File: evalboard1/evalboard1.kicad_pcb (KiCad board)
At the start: 2 copper layers, 67.5 x 45.3 mm, 36 parts, among them J1 USB_OTG, J10 Conn_01x12_Male, J11 Conn_01x18_Male, J12 Conn_01x15_Male, J13 Conn_01x03_Male, J14 power select, J2 RX, J3 TX, J4 analog, J5 IO, J6 core, J7 Conn_01x09_Male, J8 Conn_01x06_Male, J9 Conn_01x17_Male, SW1 SW_Push, U1 GA144A12, U2 FT234XD-R, U3 LTC3406ES5-1.8, U4 SST25WF080B, Y1 Crystal

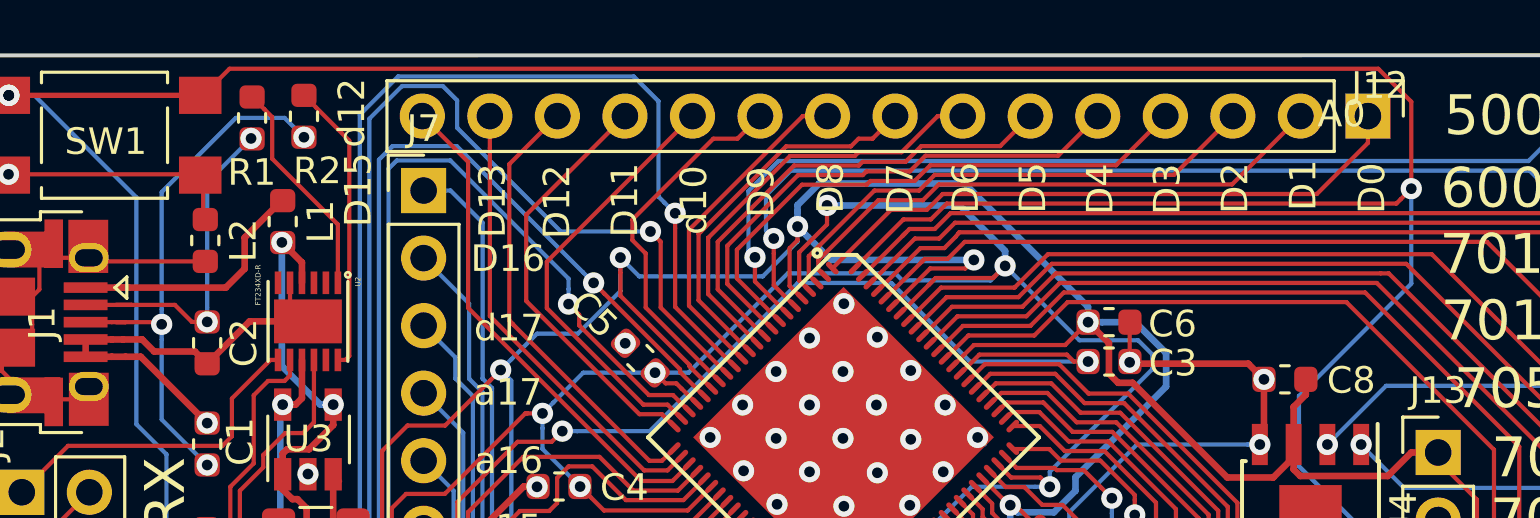
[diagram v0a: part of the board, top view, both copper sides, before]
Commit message: add pull-up resistor on RESET
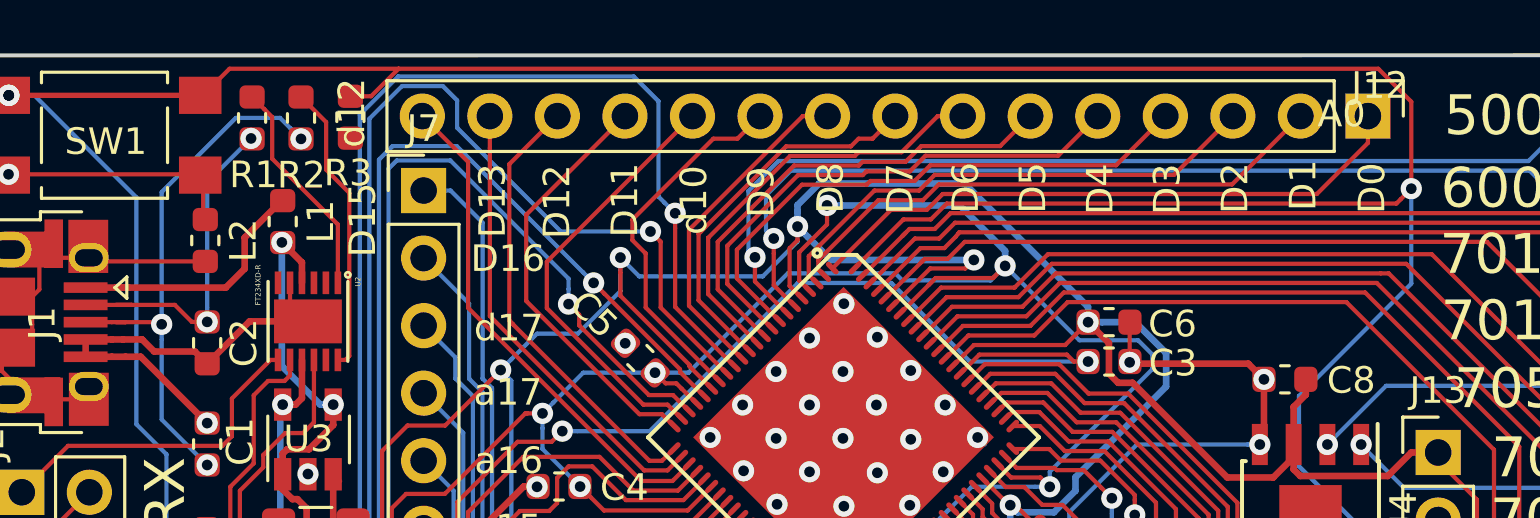
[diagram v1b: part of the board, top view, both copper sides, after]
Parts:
- added R3: 10k, Resistor_SMD:R_0603_1608Metric, F.Cu at (106.6, 75.2)
- moved R2 0.13 mm to (104.7, 75.3)
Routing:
- net RESET: track 135.7 -> 138.0 mm
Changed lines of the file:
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@@
     (thickness 1.6)
     (drawings 86)
-    (tracks 1293)
+    (tracks 1297)
     (zones 0)
-    (modules 36)
+    (modules 37)
     (nets 93)
   )
@@
   )
   (setup
-    (last_trace_width 0.25)
+    (last_trace_width 0.16)
     (user_trace_width 0.16)
     (user_trace_width 0.2)
@@
     (tags resistor)
     (attr smd)
-    (fp_text reference R1 (at -2.05 -0.01 180) (layer F.SilkS)
+    (fp_text reference R1 (at -2.13904 0.05382 180) (layer F.SilkS)
       (effects (font (size 1 1) (thickness 0.15)))
     )
@@
   )
   (module Resistor_SMD:R_0603_1608Metric (layer F.Cu)
-    (at 104.85 75.2075 90)
+    (at 104.73944 75.27046 90)
     (descr "Resistor SMD 0603 (1608 Metric), square (rectangular) end terminal, IPC_7351 nominal, (Body size source: http://www.tortai-tech.com/upload/download/2011102023233369053.pdf), generated with kicad-footprint-generator")
     (tags resistor)
     (attr smd)
-    (fp_text reference R2 (at -2.0525 0.5 180) (layer F.SilkS)
+    (fp_text reference R2 (at -2.15128 0.0127 180) (layer F.SilkS)
       (effects (font (size 1 1) (thickness 0.15)))
     )
@@
     )
   )
+  (module Resistor_SMD:R_0603_1608Metric (layer F.Cu)
+    (at 106.59618 75.24252 270)
+    (descr "Resistor SMD 0603 (1608 Metric), square (rectangular) end terminal, IPC_7351 nominal, (Body size source: http://www.tortai-tech.com/upload/download/2011102023233369053.pdf), generated with kicad-footprint-generator")
+    (tags resistor)
+    (attr smd)
+    (fp_text reference R3 (at 2.09794 0.0889) (layer F.SilkS)
+      (effects (font (size 1 1) (thickness 0.15)))
+    )
+    (fp_text value 10k (at 0 1.43 270) (layer F.Fab)
+      (effects (font (size 1 1) (thickness 0.15)))
+    )
+    (fp_line (start -0.8 0.4) (end -0.8 -0.4) (layer F.Fab) (width 0.1))
+    (fp_line (start -0.8 -0.4) (end 0.8 -0.4) (layer F.Fab) (width 0.1))
+    (fp_line (start 0.8 -0.4) (end 0.8 0.4) (layer F.Fab) (width 0.1))
+    (fp_line (start 0.8 0.4) (end -0.8 0.4) (layer F.Fab) (width 0.1))
+    (fp_line (start -0.162779 -0.51) (end 0.162779 -0.51) (layer F.SilkS) (width 0.12))
+    (fp_line (start -0.162779 0.51) (end 0.162779 0.51) (layer F.SilkS) (width 0.12))
+    (fp_line (start -1.48 0.73) (end -1.48 -0.73) (layer F.CrtYd) (width 0.05))
+    (fp_line (start -1.48 -0.73) (end 1.48 -0.73) (layer F.CrtYd) (width 0.05))
+    (fp_line (start 1.48 -0.73) (end 1.48 0.73) (layer F.CrtYd) (width 0.05))
+    (fp_line (start 1.48 0.73) (end -1.48 0.73) (layer F.CrtYd) (width 0.05))
+    (fp_text user %R (at 0 0 270) (layer F.Fab)
+      (effects (font (size 0.4 0.4) (thickness 0.06)))
+    )
+    (pad 1 smd roundrect (at -0.7875 0 270) (size 0.875 0.95) (layers F.Cu F.Paste F.Mask) (roundrect_rratio 0.25)
+      (net 52 RESET))
+    (pad 2 smd roundrect (at 0.7875 0 270) (size 0.875 0.95) (layers F.Cu F.Paste F.Mask) (roundrect_rratio 0.25)
+      (net 6 vccC))
+    (model ${KISYS3DMOD}/Resistor_SMD.3dshapes/R_0603_1608Metric.wrl
+      (at (xyz 0 0 0))
+      (scale (xyz 1 1 1))
+      (rotate (xyz 0 0 0))
+    )
+  )
   (gr_text regulated (at 101.26 117.03) (layer F.SilkS)
     (effects (font (size 0.7 0.7) (thickness 0.1)))
@@
   (gr_line (start 159.53 72.91) (end 159.54 118.18) (layer Edge.Cuts) (width 0.15))
   (gr_line (start 92 72.92) (end 159.53 72.91) (layer Edge.Cuts) (width 0.15))
-  (gr_text D15 (at 106.89 77.97 90) (layer F.SilkS)
+  (gr_text D15 (at 107.05846 79.10576 90) (layer F.SilkS)
     (effects (font (size 1 1) (thickness 0.15)))
   )
@@
     (effects (font (size 1.5 1.5) (thickness 0.2)))
   )
-  (via (at 104.85 75.994996) (size 0.8) (drill 0.4) (layers F.Cu B.Cu) (net 1))
   (via (at 101.21 88.32) (size 0.8) (drill 0.4) (layers F.Cu B.Cu) (net 1))
   (segment (start 99.5 86.61) (end 99.5 83.595695) (width 0.16) (layer B.Cu) (net 1))
   (via (at 99.5 83.03001) (size 0.8) (drill 0.4) (layers F.Cu B.Cu) (net 1))
   (segment (start 99.5 83.595695) (end 99.5 83.03001) (width 0.16) (layer B.Cu) (net 1))
-  (segment (start 104.85 75.994996) (end 104.122504 75.2675) (width 0.16) (layer B.Cu) (net 1))
   (segment (start 101.21 88.32) (end 99.5 86.61) (width 0.16) (layer B.Cu) (net 1))
-  (segment (start 99.5 82.464325) (end 99.5 83.03001) (width 0.16) (layer B.Cu) (net 1))
-  (segment (start 99.5 78.058596) (end 99.5 82.464325) (width 0.16) (layer B.Cu) (net 1))
-  (segment (start 102.291096 75.2675) (end 99.5 78.058596) (width 0.16) (layer B.Cu) (net 1))
-  (segment (start 104.122504 75.2675) (end 102.291096 75.2675) (width 0.16) (layer B.Cu) (net 1))
   (segment (start 99.41999 82.95) (end 99.5 83.03001) (width 0.16) (layer F.Cu) (net 1))
   (segment (start 97.625 82.95) (end 98.13 82.95) (width 0.16) (layer F.Cu) (net 1))
@@
   (segment (start 98.13 82.95) (end 99.41999 82.95) (width 0.16) (layer F.Cu) (net 1))
   (segment (start 97.78 82.95) (end 98.13 82.95) (width 0.16) (layer F.Cu) (net 1))
+  (via (at 104.739444 76.05796) (size 0.8) (drill 0.4) (layers F.Cu B.Cu) (net 1))
+  (segment (start 99.5 78.058596) (end 102.291096 75.2675) (width 0.16) (layer B.Cu) (net 1))
+  (segment (start 103.948984 75.2675) (end 104.339445 75.657961) (width 0.16) (layer B.Cu) (net 1))
+  (segment (start 99.5 83.03001) (end 99.5 78.058596) (width 0.16) (layer B.Cu) (net 1))
+  (segment (start 102.291096 75.2675) (end 103.948984 75.2675) (width 0.16) (layer B.Cu) (net 1))
+  (segment (start 104.339445 75.657961) (end 104.739444 76.05796) (width 0.16) (layer B.Cu) (net 1))
   (via (at 116.9289 83.7438) (size 0.8) (drill 0.4) (layers F.Cu B.Cu) (net 2))
   (via (at 105 88.66) (size 0.8) (drill 0.4) (layers F.Cu B.Cu) (net 2))
@@
   (segment (start 106.125 79.274644) (end 103.65501 76.804654) (width 0.16) (layer F.Cu) (net 49))
   (segment (start 106.125 81.47) (end 106.125 79.274644) (width 0.16) (layer F.Cu) (net 49))
-  (segment (start 105.311612 74.881612) (end 104.85 74.42) (width 0.16) (layer F.Cu) (net 50))
   (segment (start 106.41 84.37) (end 106.555001 84.224999) (width 0.16) (layer F.Cu) (net 50))
-  (segment (start 106.555001 76.125001) (end 105.311612 74.881612) (width 0.16) (layer F.Cu) (net 50))
-  (segment (start 106.555001 84.224999) (end 106.555001 76.125001) (width 0.16) (layer F.Cu) (net 50))
   (segment (start 106.125 84.37) (end 106.41 84.37) (width 0.16) (layer F.Cu) (net 50))
+  (segment (start 104.73944 74.48296) (end 105.68432 75.42784) (width 0.16) (layer F.Cu) (net 50))
+  (segment (start 105.68432 77.216539) (end 106.555001 78.08722) (width 0.16) (layer F.Cu) (net 50))
+  (segment (start 105.68432 75.42784) (end 105.68432 77.216539) (width 0.16) (layer F.Cu) (net 50))
+  (segment (start 106.555001 84.224999) (end 106.555001 78.08722) (width 0.16) (layer F.Cu) (net 50))
   (segment (start 133.634534 93.539986) (end 130.369975 90.275427) (width 0.16) (layer F.Cu) (net 51))
   (segment (start 136.075321 93.539987) (end 133.634534 93.539986) (width 0.16) (layer F.Cu) (net 51))
@@
   (segment (start 101.05 74.42) (end 100.95 74.42) (width 0.16) (layer F.Cu) (net 52))
   (segment (start 102.05 73.42) (end 101.05 74.42) (width 0.16) (layer F.Cu) (net 52))
-  (segment (start 145.25 73.42) (end 102.05 73.42) (width 0.16) (layer F.Cu) (net 52))
   (segment (start 146.49 74.66) (end 145.25 73.42) (width 0.16) (layer F.Cu) (net 52))
   (segment (start 146.49 77.93) (end 146.49 74.66) (width 0.16) (layer F.Cu) (net 52))
@@
   (segment (start 94.71 74.42) (end 98.55 78.26) (width 0.16) (layer B.Cu) (net 52))
   (segment (start 93.75 74.42) (end 94.71 74.42) (width 0.16) (layer B.Cu) (net 52))
+  (segment (start 107.37472 74.45502) (end 108.40974 73.42) (width 0.16) (layer F.Cu) (net 52))
+  (segment (start 106.59618 74.45502) (end 107.37472 74.45502) (width 0.16) (layer F.Cu) (net 52))
+  (segment (start 108.40974 73.42) (end 102.05 73.42) (width 0.16) (layer F.Cu) (net 52))
+  (segment (start 145.25 73.42) (end 108.40974 73.42) (width 0.16) (layer F.Cu) (net 52))
   (segment (start 145.193238 81.474974) (end 133.272283 81.474974) (width 0.16) (layer F.Cu) (net 56))
   (segment (start 133.272283 81.474974) (end 132.017091 82.730166) (width 0.16) (layer F.Cu) (net 56))

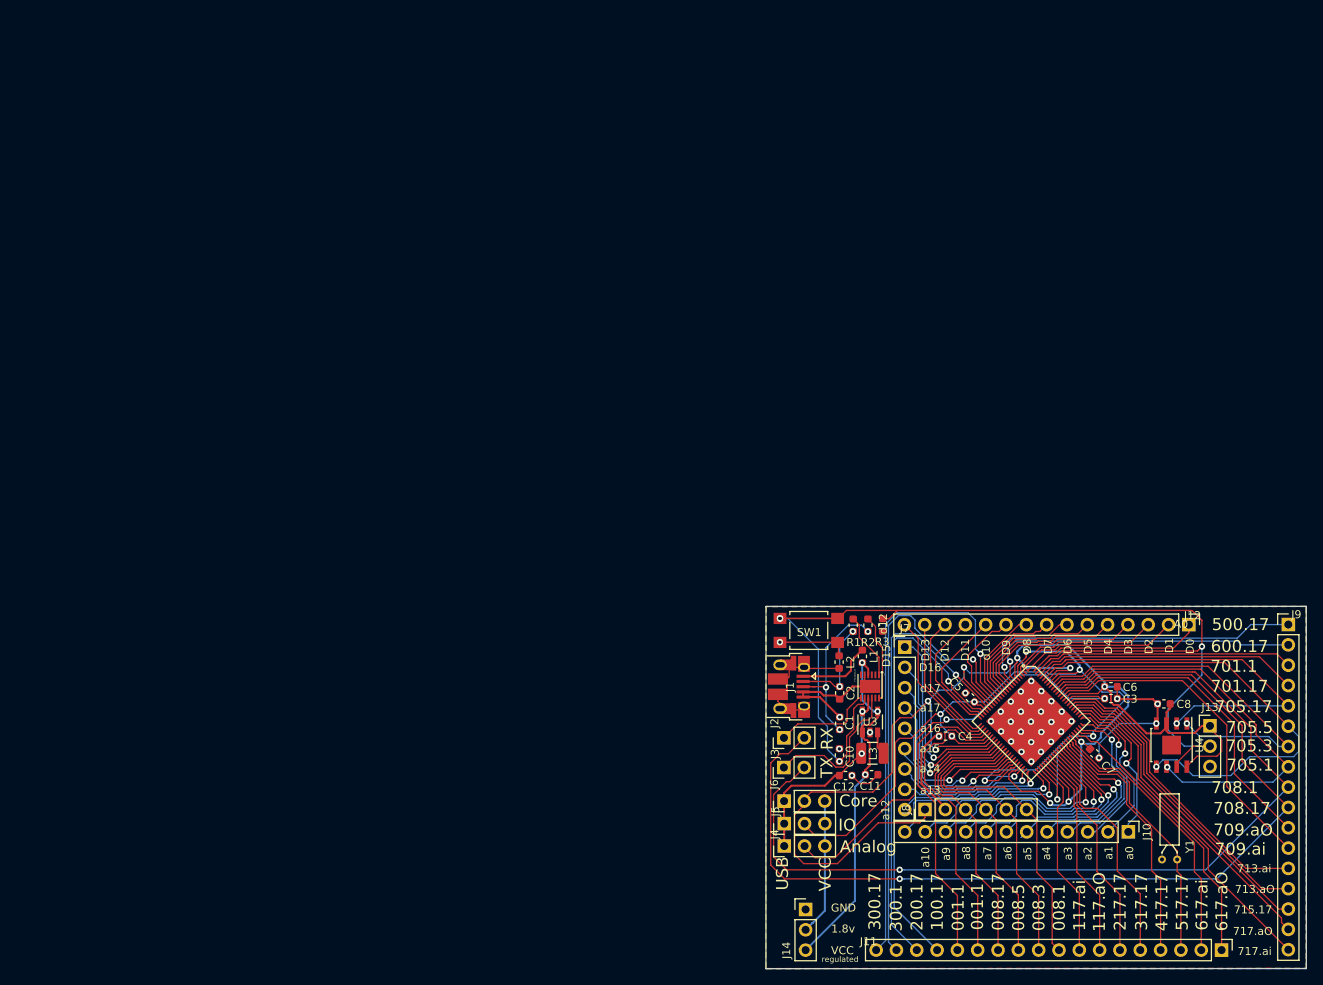
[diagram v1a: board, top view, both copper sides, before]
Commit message: replace USB micro with USB mini
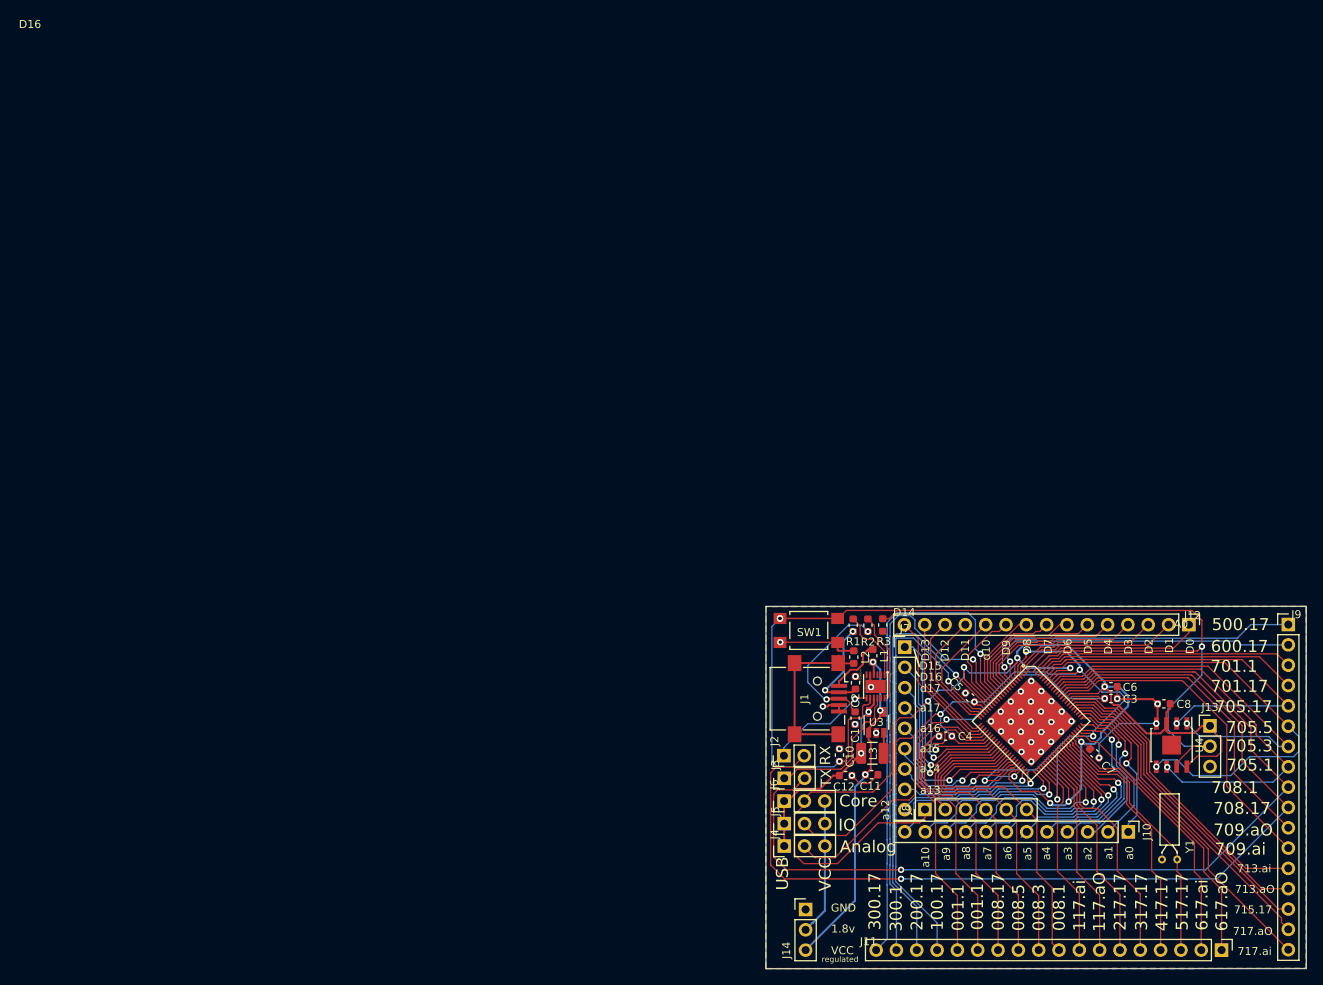
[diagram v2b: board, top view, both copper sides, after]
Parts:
- J1: footprint Connector_USB:USB_Micro-B_Amphenol_10103594-0001LF_Horizontal -> Connector_USB:USB_Mini-B_Lumberg_2486_01_Horizontal
- moved J1 3.84 mm to (98.4, 84.5)
- moved C2 2.35 mm to (103.2, 82.5), turned to 90 degrees
- moved J2 2.23 mm to (94.2, 91.6)
- moved C1 2.04 mm to (103.1, 86.9), turned to 270 degrees
- moved L2 1.94 mm to (103.0, 79.2)
- moved J3 1.35 mm to (94.3, 94.4)
- moved L1 1.30 mm to (105.3, 79.1)
- moved U3 0.78 mm to (105.8, 87.4)
- moved U2 0.70 mm to (105.7, 82.9)
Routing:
- net GND: track 63.9 -> 52.6 mm, vias 36 -> 39
- net RESET: track 138.0 -> 145.1 mm
- net Net-(J1-Pad6): track 16.2 -> 21.9 mm
- net usb1: track 9.94 -> 7.70 mm
- net 708.17: track 126.7 -> 125.1 mm
- net vcc: track 45.8 -> 44.3 mm
- net txd: track 12.5 -> 13.9 mm, vias 0 -> 1
- net Net-(R1-Pad2): track 8.32 -> 9.49 mm
- net usb3: track 20.9 -> 20.1 mm, vias 3 -> 2
- net Net-(L3-Pad1): track 3.28 -> 2.57 mm
- net 1.8v: track 28.1 -> 27.5 mm
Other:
- board text added: "D14"
- board text removed: "d12"
